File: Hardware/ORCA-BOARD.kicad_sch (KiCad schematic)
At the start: 47 parts, among them J1 Conn_01x02_Socket, J2 Conn_01x02_Socket, U1 LM5175PWPR

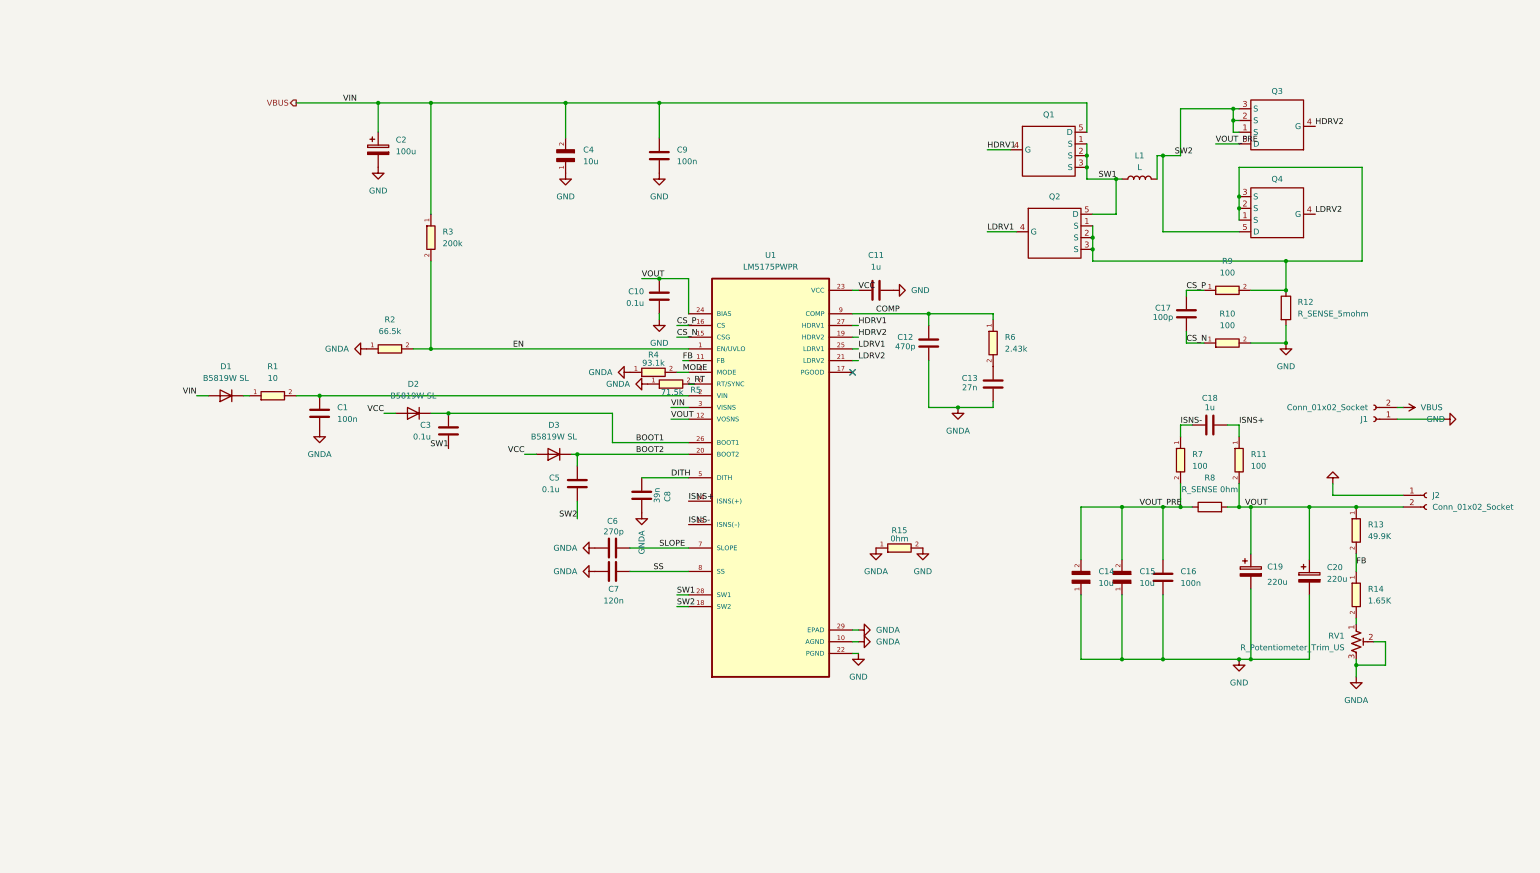
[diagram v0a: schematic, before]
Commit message: Separar placa de potencia (ORCA-Potencia) de Hardware/ORCA-BOARD de Felipe
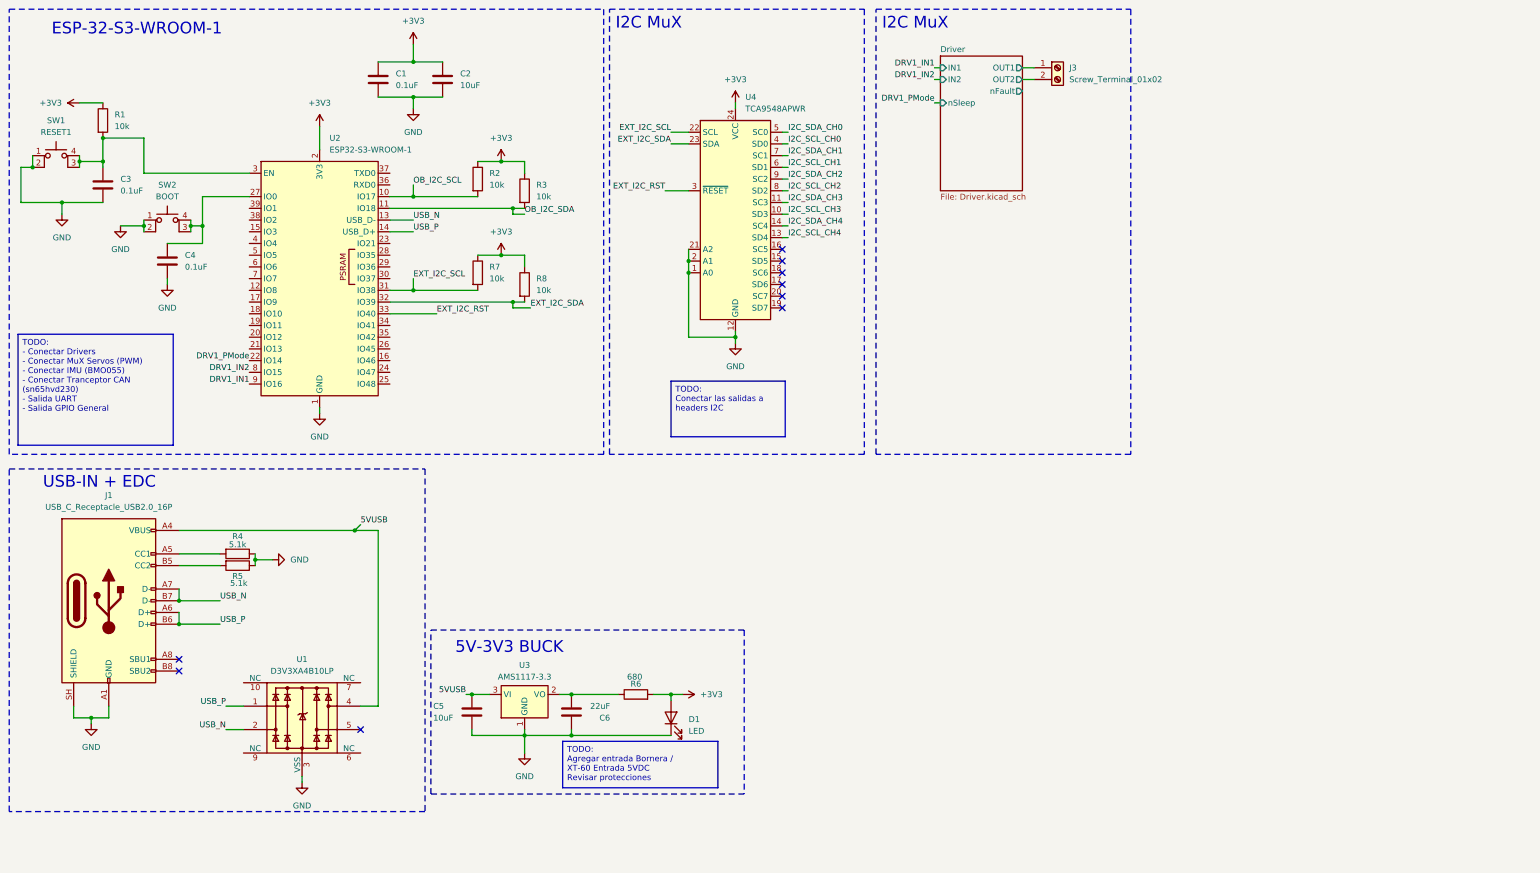
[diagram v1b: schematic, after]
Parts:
- removed C10: 0.1u, RC0603FR-1375RL:0603, symbol Device:C
- removed C11, C18: 1u, C0805X105K8RAC7210:CAPC2012X100N, symbol Device:C
- removed C12: 470p, RC0603FR-1375RL:0603, symbol Device:C
- removed C13: 27n, RC0603FR-1375RL:0603, symbol Device:C
- removed C14, C15, C4: 10u, CGA6P1X7R1E106M250AC:CAPC3225X280N, symbol CGA6P1X7R1E106M250AC:CGA6P1X7R1E106M250AC
- removed C16, C9: 100n, CGA6P1X7R1E106M250AC:CAPC3225X280N, symbol Device:C
- removed C17: 100p, RC0603FR-1375RL:0603, symbol Device:C
- removed C19, C20: 220u, Capacitor_THT:CP_Radial_D8.0mm_P3.50mm, symbol Device:C_Polarized
- removed C2: 100u, Capacitor_THT:CP_Radial_D8.0mm_P3.50mm, symbol Device:C_Polarized
- removed C7: 120n, RC0603FR-1375RL:0603, symbol Device:C
- removed C8: 39n, RC0603FR-1375RL:0603, symbol Device:C
- removed D1, D2, D3: B5819W SL, Diode_SMD:D_SOD-123, symbol Diode:1N4448W
- removed J1, J2: Conn_01x02_Socket, Connector_AMASS:AMASS_XT60-F_1x02_P7.20mm_Vertical, symbol Connector:Conn_01x02_Socket
- removed L1: L, ORCAVO:L_Pulse_PA4344, symbol Device:L
- removed Q1, Q2, Q3, Q4: (no value), Package_TO_SOT_SMD:LFPAK56, symbol LM5175PWPR:PSMN3R2-40YLD
- removed R1: 10, RC0603FR-1375RL:0603, symbol RC0603FR-1375RL:R_0603
- removed R10, R11, R7, R9: 100, RC0603FR-1375RL:0603, symbol RC0603FR-1375RL:R_0603
- removed R12: R_SENSE_5mohm, ORCAVO:R_2512_Kelvin_TLRP, symbol Device:R
- removed R13: 49.9K, RC0603FR-1375RL:0603, symbol RC0603FR-1375RL:R_0603
- removed R14: 1.65K, RC0603FR-1375RL:0603, symbol RC0603FR-1375RL:R_0603
- removed R15: 0hm, RC0603FR-1375RL:0603, symbol RC0603FR-1375RL:R_0603
- removed R2: 66.5k, RC0603FR-1375RL:0603, symbol RC0603FR-1375RL:R_0603
- removed R3: 200k, RC0603FR-1375RL:0603, symbol RC0603FR-1375RL:R_0603
- removed R4: 93.1k, RC0603FR-1375RL:0603, symbol RC0603FR-1375RL:R_0603
- removed R5: 71.5k, RC0603FR-1375RL:0603, symbol RC0603FR-1375RL:R_0603
- removed R6: 2.43k, RC0603FR-1375RL:0603, symbol RC0603FR-1375RL:R_0603
- removed RV1: R_Potentiometer_Trim_US, Potentiometer_THT:Potentiometer_Bourns_3296W_Vertical, symbol Device:R_Potentiometer_Trim_US
- removed U1: LM5175PWPR, ORCAVO:LM5175PWP, symbol LM5175PWPR:LM5175PWPR
- added C2: 10uF, Capacitor_SMD:C_1206_3216Metric_Pad1.33x1.80mm_HandSolder, symbol Device:C
- added C4: 0.1uF, Capacitor_SMD:C_0603_1608Metric_Pad1.08x0.95mm_HandSolder, symbol Device:C
- added D1: LED, LED_SMD:LED_0603_1608Metric_Pad1.05x0.95mm_HandSolder, symbol Device:LED
- added J1: USB_C_Receptacle_USB2.0_16P, symbol Connector:USB_C_Receptacle_USB2.0_16P
- added J3: Screw_Terminal_01x02, symbol Connector:Screw_Terminal_01x02
- added R1, R2, R3, R7: 10k, LED_SMD:LED_0603_1608Metric_Pad1.05x0.95mm_HandSolder, symbol Device:R
- added R4, R5: 5.1k, LED_SMD:LED_0603_1608Metric_Pad1.05x0.95mm_HandSolder, symbol Device:R
- added R6: 680, LED_SMD:LED_0603_1608Metric_Pad1.05x0.95mm_HandSolder, symbol Device:R
- added SW1: RESET1, Button_Switch_SMD:SW_MEC_5GSH9, symbol Switch:SW_MEC_5E
- added SW2: BOOT, Button_Switch_SMD:SW_MEC_5GSH9, symbol Switch:SW_MEC_5E
- added U1: D3V3XA4B10LP, Package_DFN_QFN:Diodes_UDFN-10_1x2.5mm_P0.5mm, symbol Power_Protection:D3V3XA4B10LP
- added U2: ESP32-S3-WROOM-1, RF_Module:ESP32-S3-WROOM-1, symbol RF_Module:ESP32-S3-WROOM-1
- added U3: AMS1117-3.3, Package_TO_SOT_SMD:SOT-223-3_TabPin2, symbol Regulator_Linear:AMS1117-3.3
- added U4: TCA9548APWR, Package_SO:TSSOP-24_4.4x7.8mm_P0.65mm, symbol Interface_Expansion:TCA9548APWR
- C1: value 100n -> 0.1uF; footprint RC0603FR-1375RL:0603 -> Capacitor_SMD:C_0603_1608Metric_Pad1.08x0.95mm_HandSolder
- C3: value 0.1u -> 0.1uF; footprint RC0603FR-1375RL:0603 -> Capacitor_SMD:C_0603_1608Metric_Pad1.08x0.95mm_HandSolder
- C5: value 0.1u -> 10uF; footprint RC0603FR-1375RL:0603 -> Capacitor_SMD:C_1206_3216Metric_Pad1.33x1.80mm_HandSolder
- C6: value 270p -> 22uF; footprint RC0603FR-1375RL:0603 -> Capacitor_SMD:C_1206_3216Metric_Pad1.33x1.80mm_HandSolder
- R8: value R_SENSE 0hm -> 10k; footprint 2512_RSENSE:RES_1-2176421-2 -> LED_SMD:LED_0603_1608Metric_Pad1.05x0.95mm_HandSolder
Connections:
- net GNDA is gone; now on net GND: C1.2, C6.1
- net SW1 is gone; now on net GND: C3.2
- net SW2 is gone; now on net GND: C5.2
- net VOUT_PRE is gone; now on net +3V3: R8.1
- net GND: now also C2.2, C4.1, D1.1 (K), J1.A1 (GND), J1.A12 (GND), J1.B1 (GND), J1.B12 (GND), J1.SH (SHIELD), R4.1, R5.1, SW1.1, SW1.2, SW2.1, SW2.2, U1.3 (VSS), U1.8 (VSS), U2.1 (GND), U2.40 (GND), U2.41 (GND), U3.1 (GND), U4.1 (A0), U4.12 (GND), U4.2 (A1), U4.21 (A2)
- net +3V3: now reaches C1.1
- net +3V3: now also C2.1, D1.2 (A), R1.1, R2.1, R3.1, R6.2, R7.1, U2.2 (3V3), U4.24 (VCC)
- net BOOT1: no longer names the net of C3.1
- net BOOT1: now also R1.2, SW1.3 (K), SW1.4 (A), U2.3 (EN)
- net BOOT2 renamed 5VUSB
- net 5VUSB: now also J1.A4 (VBUS), J1.A9 (VBUS), J1.B4 (VBUS), J1.B9 (VBUS), U1.4, U3.3 (VI)
- net SLOPE: no longer names the net of C6.2
- net SLOPE: now also R6.1, U3.2 (VO)
- net VOUT renamed EXT_I2C_SDA
- net EXT_I2C_SDA: now also U2.32 (IO39), U4.23 (SDA)
- new net: C4.2, SW2.3 (K), SW2.4 (A), U2.27 (IO0)
- new net: J1.B5 (CC2), R5.2
- new net: J1.A5 (CC1), R4.2
- new net DRV1_IN1: U2.9 (IO16)
- new net DRV1_IN2: U2.8 (IO15)
- new net DRV1_PMode: U2.22 (IO14)
- new net Driver/OUT1: J3.1 (Pin_1)
- new net Driver/OUT2: J3.2 (Pin_2)
- new net EXT_I2C_RST: U2.33 (IO40), U4.3 (~{RESET})
- new net EXT_I2C_SCL: R7.2, U2.31 (IO38), U4.22 (SCL)
- new net I2C_SCL_CH0: U4.4 (SD0)
- new net I2C_SCL_CH1: U4.6 (SD1)
- new net I2C_SCL_CH2: U4.8 (SD2)
- new net I2C_SCL_CH3: U4.10 (SD3)
- new net I2C_SCL_CH4: U4.13 (SD4)
- new net I2C_SDA_CH0: U4.5 (SC0)
- new net I2C_SDA_CH1: U4.7 (SC1)
- new net I2C_SDA_CH2: U4.9 (SC2)
- new net I2C_SDA_CH3: U4.11 (SC3)
- new net I2C_SDA_CH4: U4.14 (SC4)
- new net OB_I2C_SCL: R2.2, U2.10 (IO17)
- new net OB_I2C_SDA: R3.2, U2.11 (IO18)
- new net USB_N: J1.A7 (D-), J1.B7 (D-), U1.2, U2.13 (USB_D-)
- new net USB_P: J1.A6 (D+), J1.B6 (D+), U1.1, U2.14 (USB_D+)
- no-connect marks 1 -> 9
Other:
- added sheet Driver (Driver.kicad_sch)
- note added: "5V-3V3 BUCK"
- note added: "ESP-32-S3-WROOM-1"
- note added: "I2C MuX"
- note added: "USB-IN + EDC"
- company: L.A.A, J.F.A, F.G -> (none)
- title: ORCA BOARD -> (none)

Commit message: Version preeliminar blockeada Rev A PCB Control
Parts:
- removed U1: D3V3XA4B10LP, Package_DFN_QFN:Diodes_UDFN-10_1x2.5mm_P0.5mm, symbol Power_Protection:D3V3XA4B10LP
- added C13: 0.1uF, Capacitor_SMD:C_0603_1608Metric_Pad1.08x0.95mm_HandSolder, symbol Device:C
- added D2: D_SS54, Diode_SMD:D_SMA_Handsoldering, symbol Device:D_Schottky
- added D4: SMBJ5.0A, Diode_SMD:D_SMB, symbol Diode:B220
- added J14, J15, J16, J17: Conn_01x04_Pin, Connector_JST:JST_EH_B4B-EH-A_1x04_P2.50mm_Vertical, symbol Connector:Conn_01x04_Pin
- added J19, J20: Conn_01x02_Socket, Connector_AMASS:AMASS_XT60-F_1x02_P7.20mm_Vertical, symbol Connector:Conn_01x02_Socket
- added J2: Conn_01x02_Socket, Connector_JST:JST_ZH_B2B-ZR_1x02_P1.50mm_Vertical, symbol Connector:Conn_01x02_Socket
- added J4: Screw_Terminal_01x02, TerminalBlock_Phoenix:TerminalBlock_Phoenix_MPT-0,5-2-2.54_1x02_P2.54mm_Horizontal, symbol Connector:Screw_Terminal_01x02
- added J5: Conn_01x02_Socket, Connector_JST:JST_EH_B2B-EH-A_1x02_P2.50mm_Vertical, symbol Connector:Conn_01x02_Socket
- added R15: 120, LED_SMD:LED_0603_1608Metric_Pad1.05x0.95mm_HandSolder, symbol Device:R
- added R16: 1k, LED_SMD:LED_0603_1608Metric_Pad1.05x0.95mm_HandSolder, symbol Device:R
- added U1: BNO085_Adafruit, BNO085_Adafruit:BNO085_Adafruit, symbol BNO095_Adafruit:BNO085_Adafruit
- added U10: TPD4E001DBVR, footprints:DBV6-M, symbol 2026-09-08_16-07-31:TPD4E001DBVR
- added U7: SN65HVD230, Package_SO:SOIC-8_3.9x4.9mm_P1.27mm, symbol Interface_CAN_LIN:SN65HVD230
- J1: footprint (none) -> Connector_USB:USB_C_Receptacle_GCT_USB4105-xx-A_16P_TopMnt_Horizontal
- J3: footprint (none) -> TerminalBlock_Phoenix:TerminalBlock_Phoenix_MPT-0,5-2-2.54_1x02_P2.54mm_Horizontal
- SW1, SW2: footprint Button_Switch_SMD:SW_MEC_5GSH9 -> Switch_4_pins:SW_SPST_B3S-1000_1_4_labels
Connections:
- net +3V3: now also J16.2 (Pin_2), J17.2 (Pin_2), U1.1 (VIN), U7.3 (VCC)
- net 5VUSB: now also D2.2 (A), D4.1 (K); no longer C5.1, U3.3 (VI)
- net GND: now also C13.2, D4.2 (A), J14.1 (Pin_1), J15.1 (Pin_1), J16.1 (Pin_1), J17.1 (Pin_1), J19.1 (Pin_1), J20.1 (Pin_1), R16.2, U1.3 (GND), U10.2 (GND), U7.2 (GND)
- net I2C_SCL_CH0: now also J14.4 (Pin_4)
- net I2C_SCL_CH1: now also J15.4 (Pin_4)
- net I2C_SCL_CH2: now also J16.4 (Pin_4)
- net I2C_SCL_CH3: now also J17.4 (Pin_4)
- net I2C_SDA_CH0: now also J14.3 (Pin_3)
- net I2C_SDA_CH1: now also J15.3 (Pin_3)
- net I2C_SDA_CH2: now also J16.3 (Pin_3)
- net I2C_SDA_CH3: now also J17.3 (Pin_3)
- net OB_I2C_SCL: now also U1.4 (SCL)
- net OB_I2C_SDA: now also U1.5 (SDA)
- net USB_N: now also U10.1 (IO1)
- net USB_P: now also U10.3 (IO2)
- net SensCurrent_IN: now reaches U2.17 (IO9)
- net DRV2_PMode: now reaches U2.19 (IO11)
- net DRV2_IN1: now reaches U2.20 (IO12)
- net DRV2_IN2: now reaches U2.21 (IO13)
- net UART_1_Tx: now reaches U2.24 (IO47)
- net UART_1_Tx: now also J5.1 (Pin_1)
- net UART_1_Rx: now reaches U2.25 (IO48)
- net UART_1_Rx: now also J5.2 (Pin_2)
- net CAN_TX: now reaches U2.6 (IO6)
- net CAN_TX: now also U7.1 (D)
- net CAN_RX: now reaches U2.7 (IO7)
- net CAN_RX: now also U7.4 (R)
- new net: C13.1, U10.5 (VCC)
- new net: R16.1, U7.8 (Rs)
- new net: J2.1 (Pin_1), R15.1, U7.7 (CANH)
- new net: J2.2 (Pin_2), R15.2, U7.6 (CANL)
- new net 5V: C5.1, D2.1 (K), J14.2 (Pin_2), J15.2 (Pin_2), U3.3 (VI)
- new net Driver1/OUT1: J4.1 (Pin_1)
- new net Driver1/OUT2: J4.2 (Pin_2)
- new net VBUS: J19.2 (Pin_2)
- new net VM: J20.2 (Pin_2)
- no-connect marks 9 -> 20
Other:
- added sheet 2s-6s_to_5v (logic.kicad_sch)
- added sheet Driver1 (Driver.kicad_sch)
- added sheet MuxServos (MuxServos.kicad_sch)
- added sheet Sensor_corriente (Sensor_corriente.kicad_sch)
- added sheet Sensor_voltaje (Sensor_voltaje.kicad_sch)
- note added: "CAN-Transciever"
- note added: "Drivers"
- note added: "FELIPE"
- note added: "IMU-BNO085"
- note added: "MuX Servos"
- note added: "POWER (Vbat - 5V | Vm)"
- note added: "Sensor de Corriente"
- note added: "Sensor de Voltaje"
- company: (none) -> L.A.A, J.F.A, F.G
- title: (none) -> ORCA BOARD
- moved on the sheet: C6, D1, J3, R6, U3, U4
